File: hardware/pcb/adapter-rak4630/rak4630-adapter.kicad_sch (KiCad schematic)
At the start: 26 parts, among them J3 USB-C, J4 SER_SEL, J5 SER_SEL, SW1 RESET, U2 Platform_LoRa, U3 USBLC6-2SC6, U4 RAK4630-8-SM-I, U5 RV-3028-C7

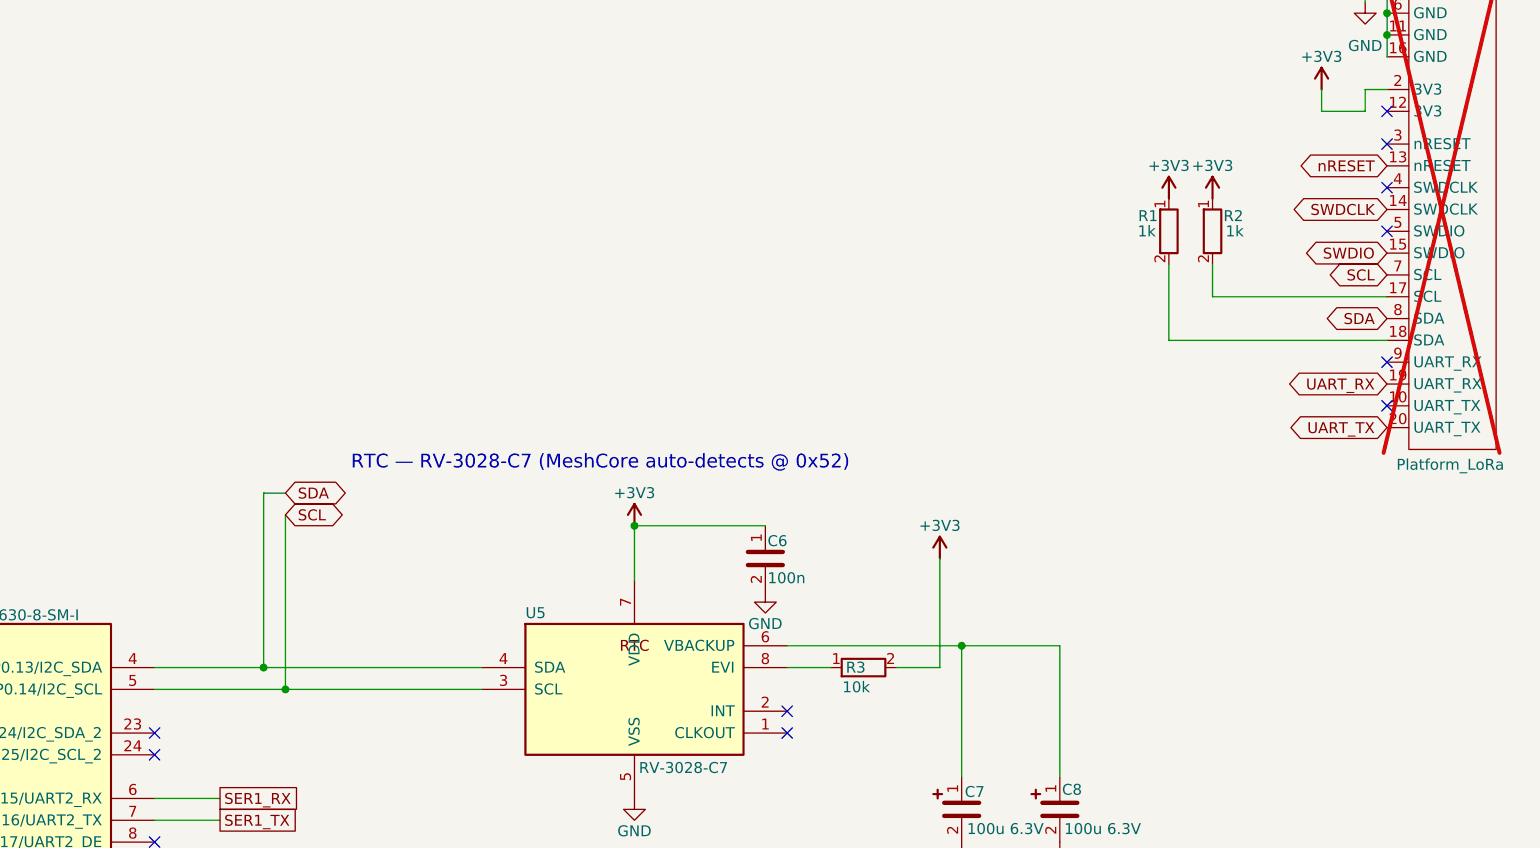
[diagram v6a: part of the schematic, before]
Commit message: Final PCB adjuments to rev 1.1
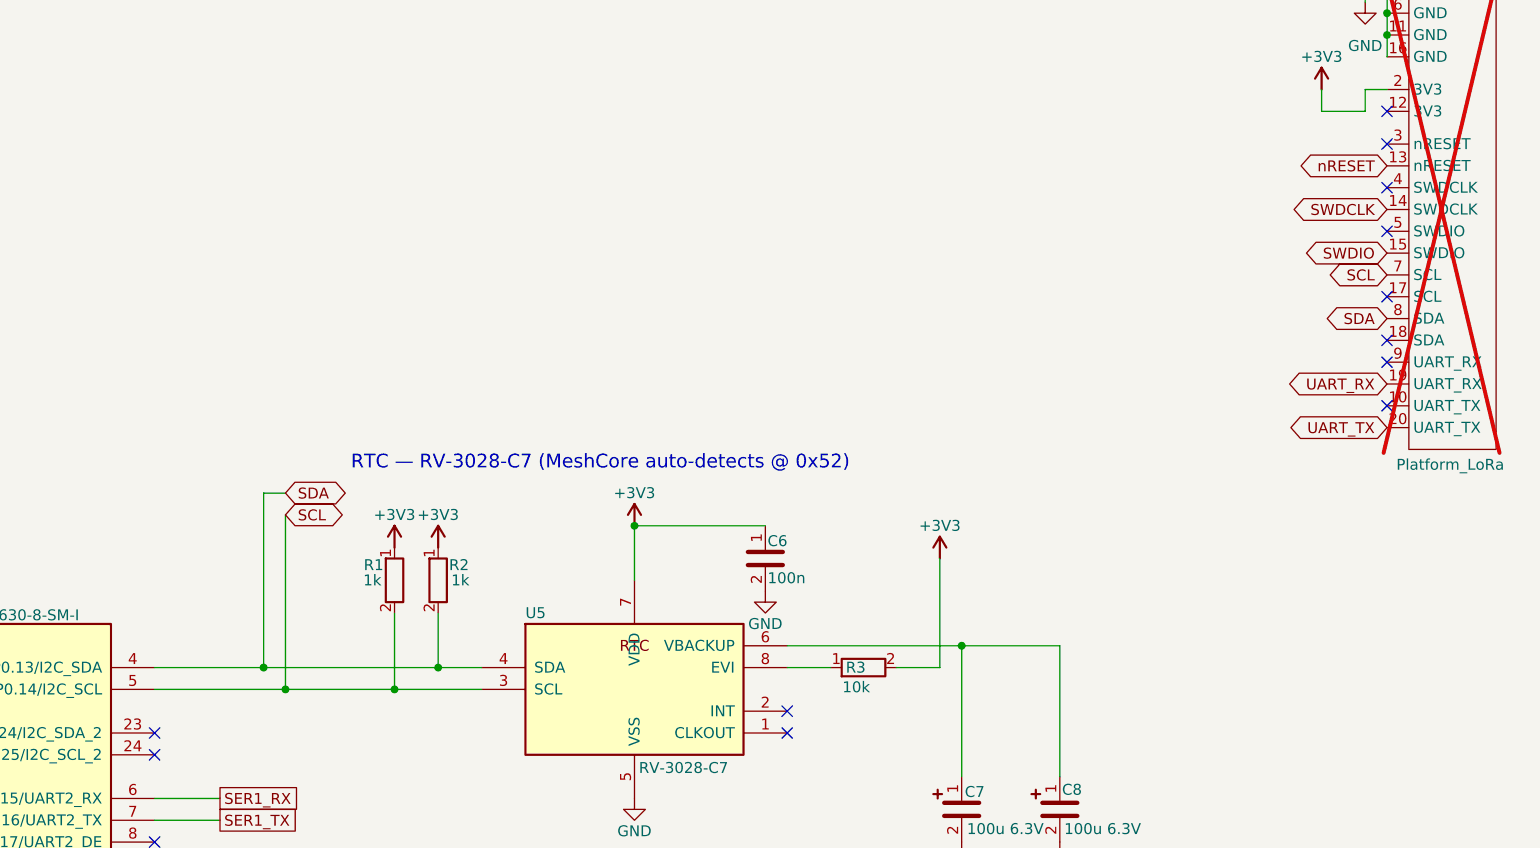
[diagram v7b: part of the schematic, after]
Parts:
- U3: FT Rotation Offset (none) -> 90; JLCPCB Rotation Offset -90 -> (none)
- U5: FT Rotation Offset (none) -> 180; JLCPCB Rotation Offset 180 -> (none)
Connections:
- net SCL: now also R1.2
- net SDA: now also R2.2
- net at U2.17 (SCL): no longer R2.2
- net at U2.18 (SDA): no longer R1.2
- no-connect marks 29 -> 31

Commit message: Parts ordered!
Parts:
- C7, C8, U5: now not fitted; now left out of the parts list
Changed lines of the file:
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@@
 		(body_style 1)
 		(exclude_from_sim no)
-		(in_bom yes)
+		(in_bom no)
 		(on_board yes)
-		(in_pos_files yes)
-		(dnp no)
+		(in_pos_files no)
+		(dnp yes)
 		(property "Reference" "C8"
 			(at 338.074 124.714 0)
@@
 		(body_style 1)
 		(exclude_from_sim no)
-		(in_bom yes)
+		(in_bom no)
 		(on_board yes)
-		(in_pos_files yes)
-		(dnp no)
+		(in_pos_files no)
+		(dnp yes)
 		(property "Reference" "U5"
 			(at 275.59 104.14 0)
@@
 		(body_style 1)
 		(exclude_from_sim no)
-		(in_bom yes)
+		(in_bom no)
 		(on_board yes)
-		(in_pos_files yes)
-		(dnp no)
+		(in_pos_files no)
+		(dnp yes)
 		(property "Reference" "C7"
 			(at 327.914 124.968 0)
